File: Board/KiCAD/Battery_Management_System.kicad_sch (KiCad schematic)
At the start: 19 parts, among them J1 Conn_01x06_Socket, J10 Conn_01x02, J11 Conn_01x02, J12 Conn_01x02, J13 Conn_01x02, J5 Conn_01x03, J7 Conn_01x05, J8 Conn_01x02, J9 Conn_01x02

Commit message: Updated schematic
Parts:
- J1: MFR Würth Elektronik -> ürth Elektronik
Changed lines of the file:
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@@
 					(size 1.27 1.27)
 				)
+				(hide yes)
 			)
 		)
@@
 					(size 1.27 1.27)
 				)
+				(hide yes)
 			)
 		)
@@
 					(size 1.27 1.27)
 				)
+				(hide yes)
 			)
 		)
@@
 					(size 1.27 1.27)
 				)
+				(hide yes)
 			)
 		)
@@
 			)
 		)
-		(property "MFR" "Würth Elektronik"
+		(property "MFR" "ürth Elektronik"
 			(at 62.23 105.41 0)
 			(effects
@@
 					(size 1.27 1.27)
 				)
+				(hide yes)
 			)
 		)
@@
 					(size 1.27 1.27)
 				)
+				(hide yes)
 			)
 		)
@@
 					(size 1.27 1.27)
 				)
+				(hide yes)
 			)
 		)
@@
 					(size 1.27 1.27)
 				)
+				(hide yes)
 			)
 		)
@@
 					(size 1.27 1.27)
 				)
+				(hide yes)
 			)
 		)
@@
 					(size 1.27 1.27)
 				)
+				(hide yes)
 			)
 		)
@@
 					(size 1.27 1.27)
 				)
+				(hide yes)
 			)
 		)
@@
 					(size 1.27 1.27)
 				)
+				(hide yes)
 			)
 		)
@@
 					(size 1.27 1.27)
 				)
+				(hide yes)
 			)
 		)
@@
 					(size 1.27 1.27)
 				)
+				(hide yes)
 			)
 		)
@@
 					(size 1.27 1.27)
 				)
+				(hide yes)
 			)
 		)
@@
 					(size 1.27 1.27)
 				)
+				(hide yes)
 			)
 		)
@@
 					(size 1.27 1.27)
 				)
+				(hide yes)
 			)
 		)
@@
 					(size 1.27 1.27)
 				)
+				(hide yes)
 			)
 		)
@@
 					(size 1.27 1.27)
 				)
+				(hide yes)
 			)
 		)
@@
 					(size 1.27 1.27)
 				)
+				(hide yes)
 			)
 		)
@@
 					(size 1.27 1.27)
 				)
+				(hide yes)
 			)
 		)
@@
 					(size 1.27 1.27)
 				)
+				(hide yes)
 			)
 		)
@@
 					(size 1.27 1.27)
 				)
+				(hide yes)
 			)
 		)
@@
 					(size 1.27 1.27)
 				)
+				(hide yes)
 			)
 		)
@@
 					(size 1.27 1.27)
 				)
+				(hide yes)
 			)
 		)
@@
 					(size 1.27 1.27)
 				)
+				(hide yes)
 			)
 		)
@@
 					(size 1.27 1.27)
 				)
-			)
-		)
+				(hide yes)
+			)
+		)

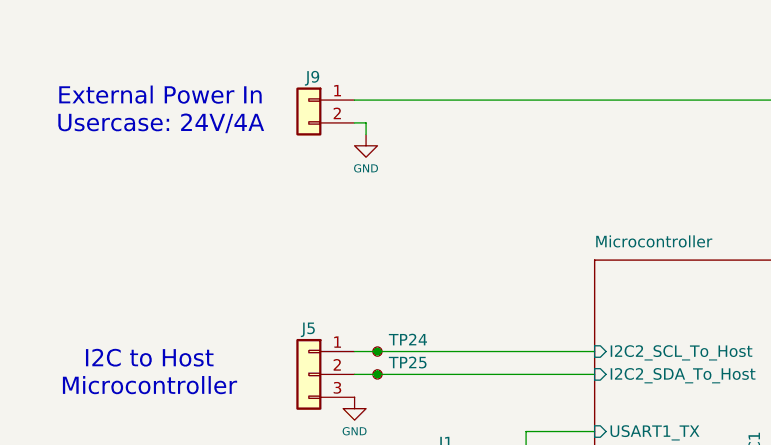
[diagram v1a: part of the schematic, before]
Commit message: PCB Optimization
Made changes to the PCB to make it smaller, as well as adding the Castellated Vias

@andrewgreenberg
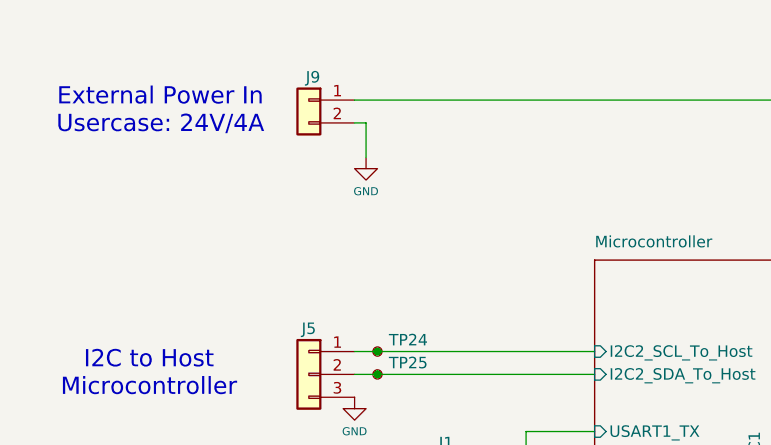
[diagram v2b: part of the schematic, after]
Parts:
- TP1, TP14, TP15, TP16, TP17, TP24, TP25, TP6, TP7, TP8: footprint TestPoint:TestPoint_THTPad_1.0x1.0mm_Drill0.5mm -> TestPoint:TestPoint_Pad_1.0x1.0mm
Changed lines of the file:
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@@
 	(wire
 		(pts
-			(xy 53.34 63.5) (xy 53.34 62.23)
+			(xy 53.34 66.04) (xy 53.34 62.23)
 		)
 		(stroke
@@
 			)
 		)
-		(property "Footprint" "TestPoint:TestPoint_THTPad_1.0x1.0mm_Drill0.5mm"
+		(property "Footprint" "TestPoint:TestPoint_Pad_1.0x1.0mm"
 			(at 151.13 87.63 0)
 			(effects
@@
 			)
 		)
-		(property "Footprint" "TestPoint:TestPoint_THTPad_1.0x1.0mm_Drill0.5mm"
+		(property "Footprint" "TestPoint:TestPoint_Pad_1.0x1.0mm"
 			(at 143.51 129.54 0)
 			(effects
@@
 			)
 		)
-		(property "Footprint" "TestPoint:TestPoint_THTPad_1.0x1.0mm_Drill0.5mm"
+		(property "Footprint" "TestPoint:TestPoint_Pad_1.0x1.0mm"
 			(at 139.7 73.66 0)
 			(effects
@@
 			)
 		)
-		(property "Footprint" "TestPoint:TestPoint_THTPad_1.0x1.0mm_Drill0.5mm"
+		(property "Footprint" "TestPoint:TestPoint_Pad_1.0x1.0mm"
 			(at 148.59 85.09 0)
 			(effects
@@
 			)
 		)
-		(property "Footprint" "TestPoint:TestPoint_THTPad_1.0x1.0mm_Drill0.5mm"
+		(property "Footprint" "TestPoint:TestPoint_Pad_1.0x1.0mm"
 			(at 59.69 87.63 0)
 			(effects
@@
 			)
 		)
-		(property "Footprint" "TestPoint:TestPoint_THTPad_1.0x1.0mm_Drill0.5mm"
+		(property "Footprint" "TestPoint:TestPoint_Pad_1.0x1.0mm"
 			(at 143.51 127 0)
 			(effects
@@
 			)
 		)
-		(property "Footprint" "TestPoint:TestPoint_THTPad_1.0x1.0mm_Drill0.5mm"
+		(property "Footprint" "TestPoint:TestPoint_Pad_1.0x1.0mm"
 			(at 59.69 90.17 0)
 			(effects
@@
 			)
 		)
-		(property "Footprint" "TestPoint:TestPoint_THTPad_1.0x1.0mm_Drill0.5mm"
+		(property "Footprint" "TestPoint:TestPoint_Pad_1.0x1.0mm"
 			(at 143.51 121.92 0)
 			(effects
@@
 			)
 		)
-		(property "Footprint" "TestPoint:TestPoint_THTPad_1.0x1.0mm_Drill0.5mm"
+		(property "Footprint" "TestPoint:TestPoint_Pad_1.0x1.0mm"
 			(at 143.51 124.46 0)
 			(effects
@@
 			)
 		)
-		(property "Footprint" "TestPoint:TestPoint_THTPad_1.0x1.0mm_Drill0.5mm"
+		(property "Footprint" "TestPoint:TestPoint_Pad_1.0x1.0mm"
 			(at 106.68 59.69 0)
 			(effects
@@
 	(symbol
 		(lib_id "power:GND")
-		(at 53.34 63.5 0)
+		(at 53.34 66.04 0)
 		(unit 1)
 		(exclude_from_sim no)
@@
 		(dnp no)
 		(property "Reference" "#PWR074"
-			(at 53.34 69.85 0)
+			(at 53.34 72.39 0)
 			(effects
 				(font
@@
 		)
 		(property "Value" "GND"
-			(at 53.34 67.31 0)
+			(at 53.34 69.85 0)
 			(effects
 				(font
@@
 		)
 		(property "Footprint" ""
-			(at 53.34 63.5 0)
+			(at 53.34 66.04 0)
 			(effects
 				(font
@@
 		)
 		(property "Datasheet" ""
-			(at 53.34 63.5 0)
+			(at 53.34 66.04 0)
 			(effects
 				(font
@@
 		)
 		(property "Description" "Power symbol creates a global label with name \"GND\" , ground"
-			(at 53.34 63.5 0)
+			(at 53.34 66.04 0)
 			(effects
 				(font

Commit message: PCB Optimization pt 2
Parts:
- removed J1: Conn_01x06_Socket, Connector_PinHeader_2.54mm:PinHeader_1x06_P2.54mm_Vertical, symbol Connector:Conn_01x06_Socket
- added J6: Conn_01x03, Connector_PinHeader_2.54mm:PinHeader_1x03_P2.54mm_Vertical, symbol Connector_Generic:Conn_01x03
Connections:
- net GND: now also J6.3 (Pin_3)
- net Microcontroller/USART1_RX: now also J6.2 (Pin_2)
- net Microcontroller/USART1_TX: now also J6.1 (Pin_1)
- no-connect marks 3 -> 0
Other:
- note added: "Serial Debug (FT232RL)"
- note removed: "Serial Debug (FT232RL 6pin)"
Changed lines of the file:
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@@
 		)
 	)
-	(text "Serial Debug\n(FT232RL 6pin)"
+	(text "Serial Debug\n(FT232RL)"
 		(exclude_from_sim no)
 		(at 44.45 106.68 0)
@@
 		(color 0 0 0 0)
 	)
-	(no_connect
-		(at 67.31 107.95)
-	)
-	(no_connect
-		(at 67.31 110.49)
-	)
-	(no_connect
-		(at 67.31 100.33)
-	)
 	(wire
 		(pts
@@
 	(wire
 		(pts
-			(xy 68.58 114.3) (xy 68.58 113.03)
+			(xy 68.58 109.22) (xy 68.58 107.95)
 		)
 		(stroke
@@
 	(wire
 		(pts
-			(xy 68.58 113.03) (xy 67.31 113.03)
+			(xy 68.58 107.95) (xy 67.31 107.95)
 		)
 		(stroke
@@
 	(symbol
 		(lib_id "power:GND")
-		(at 68.58 114.3 0)
+		(at 68.58 109.22 0)
 		(unit 1)
 		(exclude_from_sim no)
@@
 		(dnp no)
 		(property "Reference" "#PWR077"
-			(at 68.58 120.65 0)
+			(at 68.58 115.57 0)
 			(effects
 				(font
@@
 		)
 		(property "Value" "GND"
-			(at 68.58 118.11 0)
+			(at 68.58 113.03 0)
 			(effects
 				(font
@@
 		)
 		(property "Footprint" ""
-			(at 68.58 114.3 0)
+			(at 68.58 109.22 0)
 			(effects
 				(font
@@
 		)
 		(property "Datasheet" ""
-			(at 68.58 114.3 0)
+			(at 68.58 109.22 0)
 			(effects
 				(font
@@
 		)
 		(property "Description" "Power symbol creates a global label with name \"GND\" , ground"
-			(at 68.58 114.3 0)
+			(at 68.58 109.22 0)
 			(effects
 				(font
@@
 	)
 	(symbol
-		(lib_id "Connector:Conn_01x06_Socket")
-		(at 62.23 105.41 0)
-		(mirror y)
-		(unit 1)
-		(exclude_from_sim no)
-		(in_bom yes)
-		(on_board yes)
-		(dnp no)
-		(property "Reference" "J1"
-			(at 62.23 97.79 0)
-			(effects
-				(font
-					(size 1.27 1.27)
-				)
-			)
-		)
-		(property "Value" "Conn_01x06_Socket"
-			(at 58.42 97.79 0)
-			(effects
-				(font
-					(size 1.27 1.27)
-				)
-				(hide yes)
-			)
-		)
-		(property "Footprint" "Connector_PinHeader_2.54mm:PinHeader_1x06_P2.54mm_Vertical"
-			(at 62.23 105.41 0)
-			(effects
-				(font
-					(size 1.27 1.27)
-				)
-				(hide yes)
-			)
-		)
-		(property "Datasheet" "~"
-			(at 62.23 105.41 0)
-			(effects
-				(font
-					(size 1.27 1.27)
-				)
-				(hide yes)
-			)
-		)
-		(property "Description" "Generic connector, single row, 01x06, script generated"
-			(at 62.23 105.41 0)
-			(effects
-				(font
-					(size 1.27 1.27)
-				)
-				(hide yes)
-			)
-		)
-		(property "Availability" ""
-			(at 62.23 105.41 0)
-			(effects
-				(font
-					(size 1.27 1.27)
-				)
-			)
-		)
-		(property "Check_prices" ""
-			(at 62.23 105.41 0)
-			(effects
-				(font
-					(size 1.27 1.27)
-				)
-			)
-		)
-		(property "Description_1" ""
-			(at 62.23 105.41 0)
-			(effects
-				(font
-					(size 1.27 1.27)
-				)
-			)
-		)
-		(property "MANUFACTURER" ""
-			(at 62.23 105.41 0)
-			(effects
-				(font
-					(size 1.27 1.27)
-				)
-			)
-		)
-		(property "MAXIMUM_PACKAGE_HEIGHT" ""
-			(at 62.23 105.41 0)
-			(effects
-				(font
-					(size 1.27 1.27)
-				)
-			)
-		)
-		(property "PARTREV" ""
-			(at 62.23 105.41 0)
-			(effects
-				(font
-					(size 1.27 1.27)
-				)
-			)
-		)
-		(property "Package" "61300611121"
-			(at 62.23 105.41 0)
-			(effects
-				(font
-					(size 1.27 1.27)
-				)
-				(hide yes)
-			)
-		)
-		(property "Price" ""
-			(at 62.23 105.41 0)
-			(effects
-				(font
-					(size 1.27 1.27)
-				)
-			)
-		)
-		(property "SNAPEDA_PN" ""
-			(at 62.23 105.41 0)
-			(effects
-				(font
-					(size 1.27 1.27)
-				)
-			)
-		)
-		(property "STANDARD" ""
-			(at 62.23 105.41 0)
-			(effects
-				(font
-					(size 1.27 1.27)
-				)
-			)
-		)
-		(property "SnapEDA_Link" ""
-			(at 62.23 105.41 0)
-			(effects
-				(font
-					(size 1.27 1.27)
-				)
-			)
-		)
-		(property "MFR" "ürth Elektronik"
-			(at 62.23 105.41 0)
-			(effects
-				(font
-					(size 1.27 1.27)
-				)
-				(hide yes)
-			)
-		)
-		(property "MPN" "732-5319-ND"
-			(at 62.23 105.41 0)
-			(effects
-				(font
-					(size 1.27 1.27)
-				)
-				(hide yes)
-			)
-		)
-		(pin "6"
-		)
-		(pin "1"
-		)
-		(pin "4"
-		)
-		(pin "5"
-		)
-		(pin "2"
-		)
-		(pin "3"
-		)
-		(instances
-			(project ""
-				(path "/1ea1a1f5-2618-4570-85b6-e164c8f0e76f"
-					(reference "J1")
-					(unit 1)
-				)
-			)
-		)
-	)
-	(symbol
 		(lib_id "Connector_Generic:Conn_01x02")
 		(at 113.03 146.05 0)
@@
 					(unit 1)
 				)
+			)
+		)
+	)
+	(symbol
+		(lib_id "Connector_Generic:Conn_01x03")
+		(at 62.23 105.41 0)
+		(mirror y)
+		(unit 1)
+		(exclude_from_sim no)
+		(in_bom yes)
+		(on_board yes)
+		(dnp no)
+		(property "Reference" "J6"
+			(at 62.23 100.33 0)
+			(effects
+				(font
+					(size 1.27 1.27)
+				)
+			)
+		)
+		(property "Value" "Conn_01x03"
+			(at 62.23 99.06 0)
+			(effects
+				(font
+					(size 1.27 1.27)
+				)
+				(hide yes)
+			)
+		)
+		(property "Footprint" "Connector_PinHeader_2.54mm:PinHeader_1x03_P2.54mm_Vertical"
+			(at 62.23 105.41 0)
+			(effects
+				(font
+					(size 1.27 1.27)
+				)
+				(hide yes)
+			)
+		)
+		(property "Datasheet" "~"
+			(at 62.23 105.41 0)
+			(effects
+				(font
+					(size 1.27 1.27)
+				)
+				(hide yes)
+			)
+		)
+		(property "Description" "Generic connector, single row, 01x03, script generated (kicad-library-utils/schlib/autogen/connector/)"
+			(at 62.23 105.41 0)
+			(effects
+				(font
+					(size 1.27 1.27)
+				)
+				(hide yes)
+			)
+		)
+		(property "Availability" ""
+			(at 62.23 105.41 0)
+			(effects
+				(font
+					(size 1.27 1.27)
+				)
+			)
+		)
+		(property "Check_prices" ""
+			(at 62.23 105.41 0)
+			(effects
+				(font
+					(size 1.27 1.27)
+				)
+			)
+		)
+		(property "Description_1" ""
+			(at 62.23 105.41 0)
+			(effects
+				(font
+					(size 1.27 1.27)
+				)
+			)
+		)
+		(property "MANUFACTURER" ""
+			(at 62.23 105.41 0)
+			(effects
+				(font
+					(size 1.27 1.27)
+				)
+			)
+		)
+		(property "MAXIMUM_PACKAGE_HEIGHT" ""
+			(at 62.23 105.41 0)
+			(effects
+				(font
+					(size 1.27 1.27)
+				)
+			)
+		)
+		(property "PARTREV" ""
+			(at 62.23 105.41 0)
+			(effects
+				(font
+					(size 1.27 1.27)
+				)
+			)
+		)
+		(property "Package" "61300311121"
+			(at 55.372 112.522 0)
+			(effects
+				(font
+					(size 1.27 1.27)
+				)
+				(hide yes)
+			)
+		)
+		(property "Price" ""
+			(at 62.23 105.41 0)
+			(effects
+				(font
+					(size 1.27 1.27)
+				)
+			)
+		)
+		(property "SNAPEDA_PN" ""
+			(at 62.23 105.41 0)
+			(effects
+				(font
+					(size 1.27 1.27)
+				)
+			)
+		)
+		(property "STANDARD" ""
+			(at 62.23 105.41 0)
+			(effects
+				(font
+					(size 1.27 1.27)
+				)
+			)
+		)
+		(property "SnapEDA_Link" ""
+			(at 62.23 105.41 0)
+			(effects
+				(font
+					(size 1.27 1.27)
+				)
+			)
+		)
+		(property "MFR" "Würth Elektronik"
+			(at 61.468 97.79 0)
+			(effects
+				(font
+					(size 1.27 1.27)
+				)
+				(hide yes)
+			)
+		)
+		(property "MPN" "732-5316-ND"
+			(at 62.23 114.808 0)
+			(effects
+				(font
+					(size 1.27 1.27)
+				)
+				(hide yes)
+			)
+		)
+		(pin "2"
+		)
+		(pin "3"
+		)
+		(pin "1"
+		)
+		(instances
+			(project "Battery_Management_System"
+				(path "/1ea1a1f5-2618-4570-85b6-e164c8f0e76f"
+					(reference "J6")
+					(unit 1)
+				)
